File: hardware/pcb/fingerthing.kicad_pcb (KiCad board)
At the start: 4 copper layers, 34 x 48 mm, 47 parts, among them J1 DX07S016JA1R1500, J2 R503, J4 SM03B-SRSS-TB(LF)(SN), SW1 434133025816, SW3 434133025816, U1 RP2350A, U2 NCP1117ST33T3G, U3 W25Q128JVSIQ, U4 USBLC6-2SC6, X1 12MHz

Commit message: 3v3 regulator / capacitor routing
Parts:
- U2: value NCP1117ST33T3G -> AP2112K-3.3; footprint RPI_COMPILED:onsemi_ncp1117st33t3g -> Package_TO_SOT_SMD:SOT-23-5
- moved C1 8.55 mm to (22.5, 14.1), turned to 180 degrees
- moved C5 4.95 mm to (30.5, 16.5)
- turned U2 to 0 degrees
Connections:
- U2 pad 1: /GND -> /VBUS
- U2 pad 2: /+3V3 -> /GND
- U2 pad 4: /+3V3 -> unconnected-(U2-NC-Pad4)
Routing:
- net /+3V3: track 41.4 -> 35.1 mm

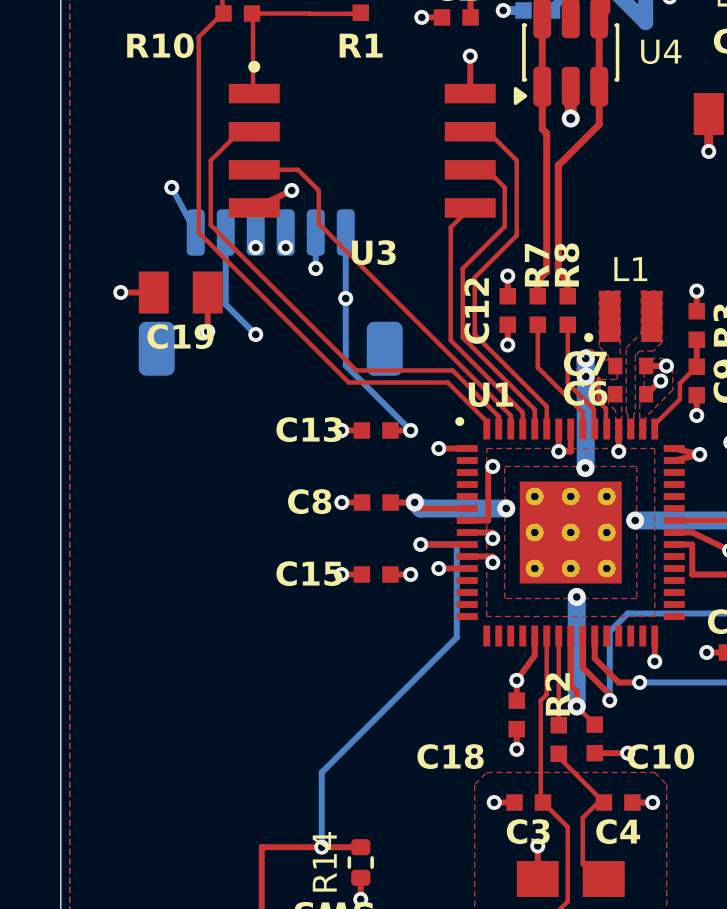
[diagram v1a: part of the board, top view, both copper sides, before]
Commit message: sensor switch / pcb
TPS22919DCKR switches both R503 supplies from GP8. Added input and output bypass, ON pull-down and switched RX pull-up. The QOD pin uses a passive symbol type for its connection to OUT. ERC, DRC and schematic parity pass with zero unconnected items. Firmware control and physical power checks remain.
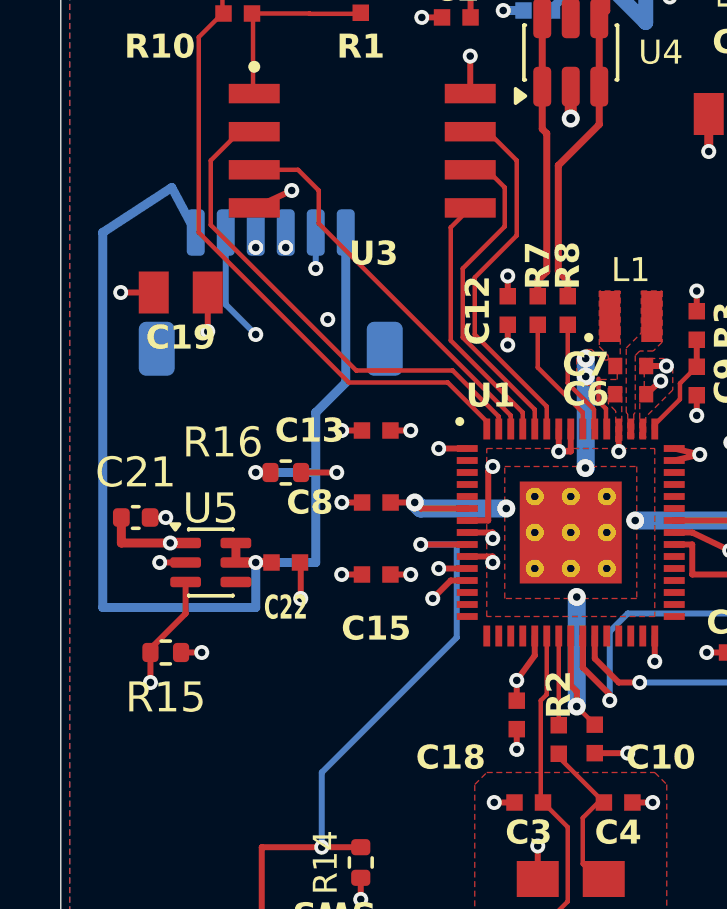
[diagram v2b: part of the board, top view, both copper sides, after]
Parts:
- added C21: 1u, Capacitor_SMD:C_0402_1005Metric, F.Cu at (2.50, 27.5)
- added C22: 100n, RPI_COMPILED:generic_capc1005x50, F.Cu at (7.50, 29.0)
- added R15: 100k, Resistor_SMD:R_0402_1005Metric, F.Cu at (3.50, 32.0)
- added R16: 10k, Resistor_SMD:R_0402_1005Metric, F.Cu at (7.50, 26.0)
- added U5: TPS22919DCK, Package_TO_SOT_SMD:SOT-363_SC-70-6, F.Cu at (5.00, 29.0)
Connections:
- J2 pad 1: /+3V3 -> /SENSOR_3V3
- J2 pad 6: /+3V3 -> /SENSOR_3V3
- U1 pad 12: unconnected-(U1-GPIO8-Pad12) -> /GPIO8
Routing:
- net /SENSOR_3V3: track 0.00 -> 41.3 mm, vias 0 -> 2
- net /GPIO8: track 0.00 -> 19.4 mm, vias 0 -> 2
- net /GPIO4: track 14.0 -> 20.5 mm, vias 2 -> 4
- net /+3V3: track 35.1 -> 28.9 mm, vias 23 -> 22
- net /GND: track 33.0 -> 36.3 mm, vias 36 -> 40

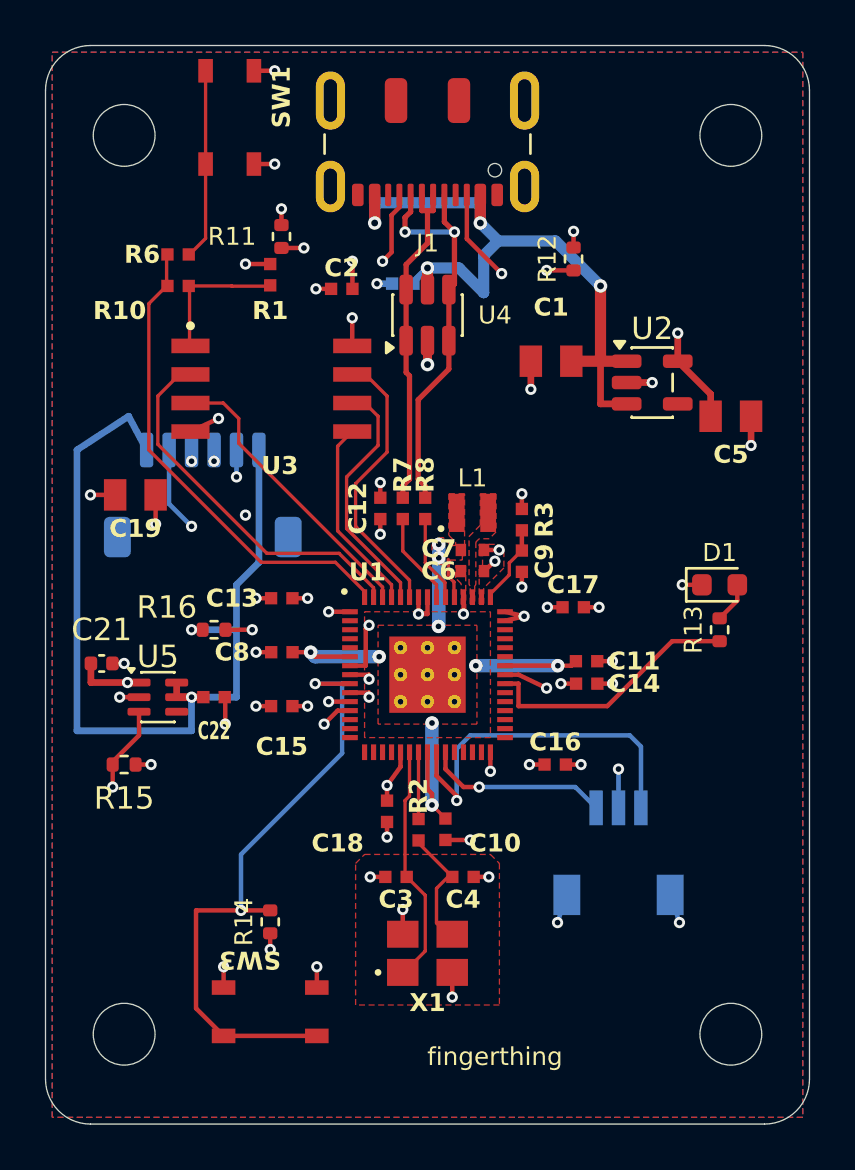
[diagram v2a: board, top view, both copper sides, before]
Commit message: switch routing / labels
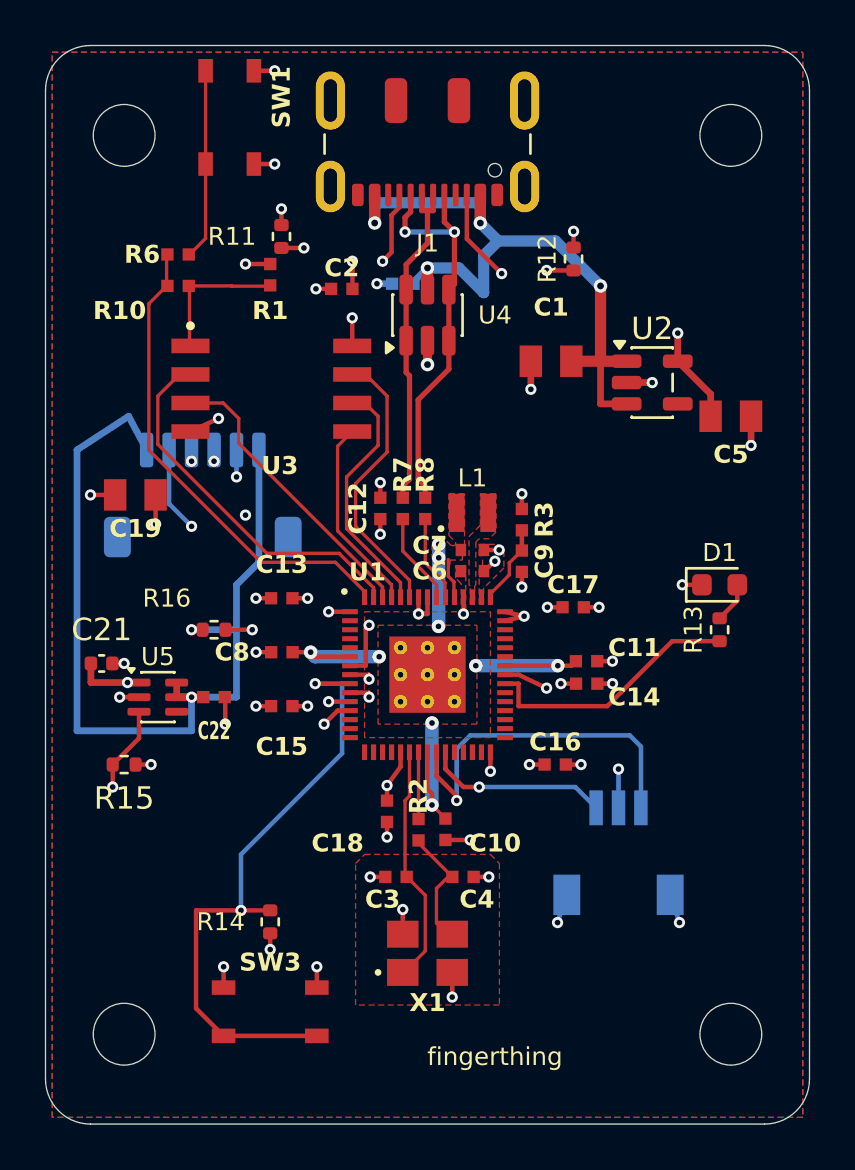
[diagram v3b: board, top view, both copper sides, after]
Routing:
- net /GPIO8: track 19.4 -> 15.8 mm
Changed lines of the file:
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@@
 		(at 24.085 28.4)
 		(property "Reference" "C14"
-			(at 2.115 0 0)
+			(at 2.115 0.6 0)
 			(unlocked yes)
 			(layer "F.SilkS")
@@
 		(at 10.515 24.6 180)
 		(property "Reference" "C13"
-			(at 2.215 0 0)
+			(at 0 1.5 0)
 			(unlocked yes)
 			(layer "F.SilkS")
@@
 		(at 19 22.45)
 		(property "Reference" "C7"
-			(at -1.5 -0.05 0)
+			(at -1.9 -0.2 0)
 			(unlocked yes)
 			(layer "F.SilkS")
@@
 		(tags "resistor")
 		(property "Reference" "R16"
-			(at -2.1 -1 0)
+			(at -2.1 -1.4 0)
 			(layer "F.SilkS")
 			(effects
 				(font
-					(size 1 1)
-					(thickness 0.15)
+					(size 0.8 0.8)
+					(thickness 0.12)
 				)
 			)
@@
 		(tags "resistor")
 		(property "Reference" "R14"
-			(at 0 -1.17 90)
+			(at 0 -2.2 0)
 			(layer "F.SilkS")
 			(effects
@@
 		(at 10 43)
 		(property "Reference" "SW3"
-			(at -0.9 -2.3 180)
+			(at 0 -2.2 0)
 			(unlocked yes)
 			(layer "F.SilkS")
@@
 			(effects
 				(font
-					(size 1 1)
-					(thickness 0.15)
+					(size 0.8 0.8)
+					(thickness 0.12)
 				)
 			)
@@
 		(at 15.6 37 180)
 		(property "Reference" "C3"
-			(at 0 -1 0)
+			(at 0.6 -1 0)
 			(unlocked yes)
 			(layer "F.SilkS")
@@
 		(at 19 23.39)
 		(property "Reference" "C6"
-			(at -1.5 0 0)
+			(at -1.9 0 0)
 			(unlocked yes)
 			(layer "F.SilkS")
@@
 		(at 24.08 27.4)
 		(property "Reference" "C11"
-			(at 2.115 0 0)
+			(at 2.12 -0.6 0)
 			(unlocked yes)
 			(layer "F.SilkS")
@@
 		(at 18.58 37)
 		(property "Reference" "C4"
-			(at 0 1 0)
+			(at 0.62 1 0)
 			(unlocked yes)
 			(layer "F.SilkS")
@@
 	)
 	(segment
-		(start 4.1625 30.7)
-		(end 2.99 31.8725)
+		(start 4.1625 30.8275)
+		(end 2.99 32)
 		(width 0.2)
 		(layer "F.Cu")
@@
 	(segment
 		(start 4.1625 29.65)
-		(end 4.1625 30.7)
-		(width 0.2)
-		(layer "F.Cu")
-		(net "/GPIO8")
-	)
-	(segment
-		(start 2.99 31.8725)
-		(end 2.99 32)
+		(end 4.1625 30.8275)
 		(width 0.2)
 		(layer "F.Cu")
@@
 	)
 	(segment
-		(start 12.4 31.2)
-		(end 7 31.2)
-		(width 0.15)
-		(layer "In2.Cu")
-		(net "/GPIO8")
-	)
-	(segment
-		(start 7 34)
-		(end 2.99 34)
+		(start 12.4 30.2)
+		(end 11.4 31.2)
 		(width 0.15)
 		(layer "In2.Cu")
@@
 	)
 	(segment
-		(start 7 31.2)
-		(end 7 34)
+		(start 5.2 33)
+		(end 2.99 33)
 		(width 0.15)
 		(layer "In2.Cu")
@@
 	)
 	(segment
-		(start 2.99 34)
-		(end 2.99 33)
+		(start 11.4 31.2)
+		(end 7 31.2)
 		(width 0.15)
 		(layer "In2.Cu")
@@
 	)
 	(segment
-		(start 12.4 30.2)
-		(end 12.4 31.2)
+		(start 7 31.2)
+		(end 5.2 33)
 		(width 0.15)
 		(layer "In2.Cu")
